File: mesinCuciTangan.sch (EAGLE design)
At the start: 9 parts, among them X1 PIR, X2 POWER, X3 IR1, X4 IR2

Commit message: Skema Beta V0.1
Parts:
- removed U$1: CP8-ADJ, userlib:CP8-ADJ
- added JP1: 12VOUTLET, pinhead:PINHD-1X5
- added JP2: GNDOUTLET, pinhead:PINHD-1X5
- added JP3: 5VOUTLET, pinhead:PINHD-1X5
- added LM2596: LM2596, userlib:CP8-ADJ
- added R1: 1K, rcl:R-US_0207/10
- added SPK_L, SPK_R: (no value), con-wago-500:W237-102
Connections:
- new net +12V: JP1.1, JP1.2, JP1.3, JP1.4, JP1.5, LM2596.IN+, X2-1.KL
- new net +5V: ARDUINO_NANO1.5V, JP3.1, JP3.2, JP3.3, JP3.4, JP3.5, LM2596.OUT+, MOD1.+5V, U$2.VCC, U$3.2, X1-1.S, X3-1.S, X4-1.S
- new net A0: ARDUINO_NANO1.ADC0/A0, U$3.4
- new net A1: ARDUINO_NANO1.ADC1/A1, U$3.5
- new net A2: ARDUINO_NANO1.ADC2/A2, U$3.6
- new net D10: ARDUINO_NANO1.D10/OC1B/!SS, U$2.TX
- new net D11: ARDUINO_NANO1.D11/MOSI, R1.1
- new net D2: ARDUINO_NANO1.D2/INT0, X1-2.S
- new net D3: ARDUINO_NANO1.D3/INT1, X3-2.S
- new net D4: ARDUINO_NANO1.D4/T0, X4-2.S
- new net GND: ARDUINO_NANO1.GND@2, JP2.1, JP2.2, JP2.3, JP2.4, JP2.5, LM2596.IN-, LM2596.OUT-, MOD1.GND@1, MOD1.GND@2, U$2.GND_1, U$3.3, X1-3.S, X2-2.KL, X3-3.S, X4-3.S
- new net N$1: MOD1.+OR, SPK_R-1.KL
- new net N$2: MOD1.IL, U$2.DAC_L
- new net N$3: MOD1.IR, U$2.DAC_R
- new net N$4: MOD1.-OR, SPK_R-2.KL
- new net N$5: MOD1.-OL, SPK_L-2.KL
- new net N$6: MOD1.+OL, SPK_L-1.KL
- new net N$7: R1.2, U$2.RX
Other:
- note added: "3 CH Relay Untuk Pompa dan Solenoid"
- note added: "Arduino NANO"
- note added: "DF Player & PAM8203"
- note added: "POWER IN & OUTLET"
- note added: "Sensor IR1"
- note added: "Sensor IR2"
- note added: "Sensor PIR"
- note added: "Sensor PIR dan IR"
- note added: "dari Power Supply"
- moved on the sheet: ARDUINO_NANO1, MOD1, U$3, X1-1, X1-2, X1-3, X2-1, X2-2, X3-1, X3-2, X3-3, X4-1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

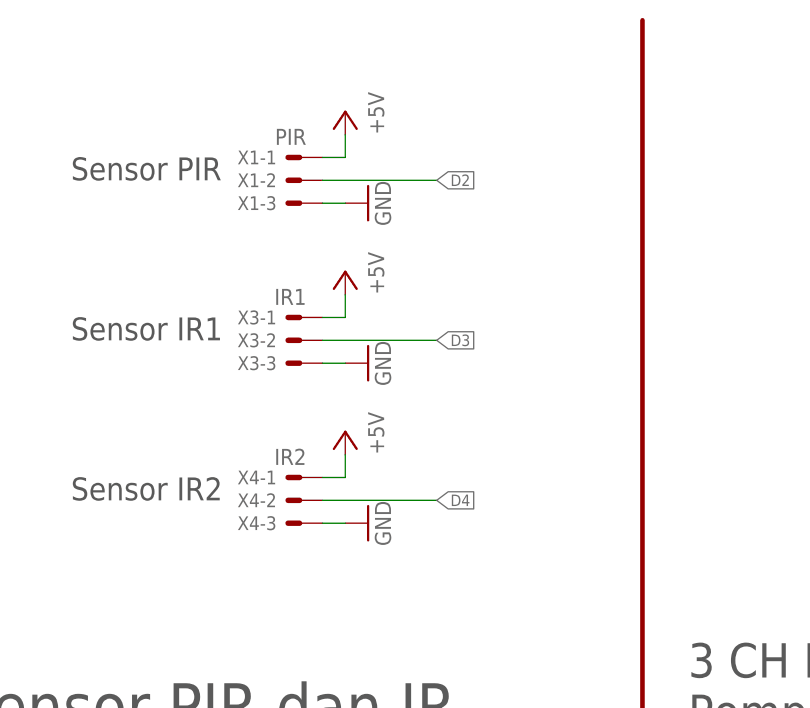
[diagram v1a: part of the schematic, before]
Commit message: simple Route Without jumper
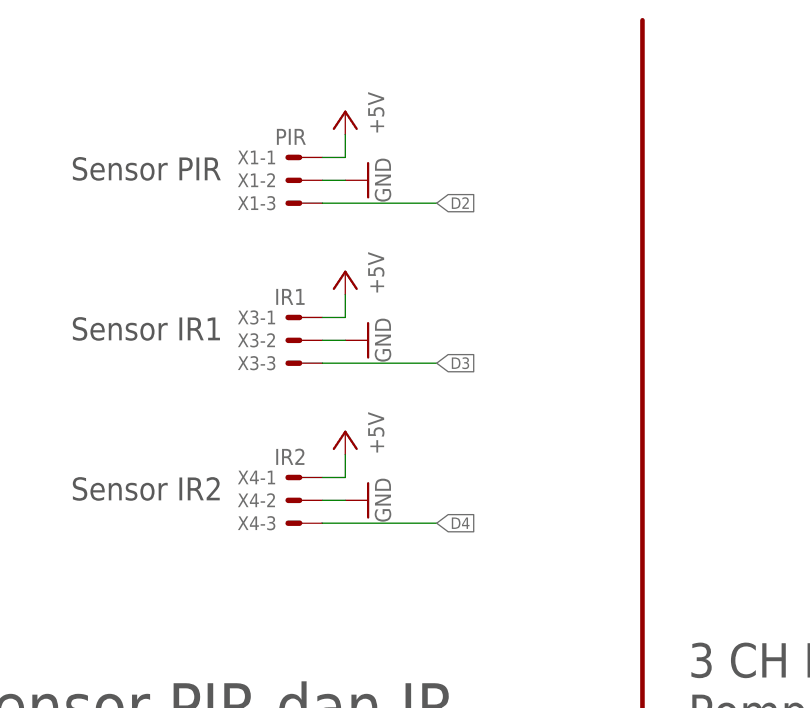
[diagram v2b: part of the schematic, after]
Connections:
- net D2: now also X1-3.S; no longer X1-2.S
- net D3: now also X3-3.S; no longer X3-2.S
- net D4: now also X4-3.S; no longer X4-2.S
- net GND: now also X1-2.S, X3-2.S, X4-2.S; no longer X1-3.S, X3-3.S, X4-3.S
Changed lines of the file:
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@@
 <setting verticaltext="up"/>
 </settings>
-<grid distance="0.1" unitdist="inch" unit="inch" style="lines" multiple="1" display="yes" altdistance="0.01" altunitdist="inch" altunit="inch"/>
+<grid distance="0.1" unitdist="inch" unit="inch" style="lines" multiple="1" display="no" altdistance="0.01" altunitdist="inch" altunit="inch"/>
 <layers>
 <layer number="1" name="Top" color="4" fill="10" visible="no" active="no"/>
@@
 <part name="LM2596" library="userlib" deviceset="CP8-ADJ" device="" value="LM2596"/>
 <part name="ARDUINO_NANO1" library="ArduinoNanoV30" deviceset="ARDUINO_NANO" device=""/>
-<part name="X2" library="con-wago-500" library_urn="urn:adsk.eagle:library:195" deviceset="W237-102" device="" package3d_urn="urn:adsk.eagle:package:10688/1" value="POWER"/>
+<part name="X2" library="con-wago-500" deviceset="W237-102" device="" package3d_urn="urn:adsk.eagle:package:10688/1" value="POWER"/>
 <part name="X3" library="con-molex" library_urn="urn:adsk.eagle:library:165" deviceset="22-23-2031" device="" package3d_urn="urn:adsk.eagle:package:8078634/1" value="IR1"/>
 <part name="X4" library="con-molex" library_urn="urn:adsk.eagle:library:165" deviceset="22-23-2031" device="" package3d_urn="urn:adsk.eagle:package:8078634/1" value="IR2"/>
@@
 <part name="GND4" library="supply1" library_urn="urn:adsk.eagle:library:371" deviceset="GND" device=""/>
 <part name="P+5" library="supply1" library_urn="urn:adsk.eagle:library:371" deviceset="+5V" device=""/>
-<part name="SPK_L" library="con-wago-500" library_urn="urn:adsk.eagle:library:195" deviceset="W237-102" device="" package3d_urn="urn:adsk.eagle:package:10688/1"/>
-<part name="SPK_R" library="con-wago-500" library_urn="urn:adsk.eagle:library:195" deviceset="W237-102" device="" package3d_urn="urn:adsk.eagle:package:10688/1"/>
+<part name="SPK_L" library="con-wago-500" deviceset="W237-102" device="" package3d_urn="urn:adsk.eagle:package:10688/1"/>
+<part name="SPK_R" library="con-wago-500" deviceset="W237-102" device="" package3d_urn="urn:adsk.eagle:package:10688/1"/>
 <part name="R1" library="rcl" deviceset="R-US_" device="0207/10" package3d_urn="urn:adsk.eagle:package:23491/2" value="1K"/>
 <part name="P+6" library="supply1" library_urn="urn:adsk.eagle:library:371" deviceset="+5V" device=""/>
@@
 <part name="P+9" library="supply1" library_urn="urn:adsk.eagle:library:371" deviceset="+5V" device=""/>
 <part name="P+10" library="supply1" library_urn="urn:adsk.eagle:library:371" deviceset="+5V" device=""/>
+<part name="P+11" library="supply1" library_urn="urn:adsk.eagle:library:371" deviceset="+5V" device=""/>
+<part name="GND10" library="supply1" library_urn="urn:adsk.eagle:library:371" deviceset="GND" device=""/>
+<part name="FRAME2" library="frames" library_urn="urn:adsk.eagle:library:229" deviceset="A4L-LOC" device=""/>
 <part name="GND7" library="supply1" library_urn="urn:adsk.eagle:library:371" deviceset="GND" device=""/>
 <part name="GND8" library="supply1" library_urn="urn:adsk.eagle:library:371" deviceset="GND" device=""/>
 <part name="GND9" library="supply1" library_urn="urn:adsk.eagle:library:371" deviceset="GND" device=""/>
-<part name="P+11" library="supply1" library_urn="urn:adsk.eagle:library:371" deviceset="+5V" device=""/>
-<part name="GND10" library="supply1" library_urn="urn:adsk.eagle:library:371" deviceset="GND" device=""/>
-<part name="FRAME2" library="frames" library_urn="urn:adsk.eagle:library:229" deviceset="A4L-LOC" device=""/>
 </parts>
 <sheets>
@@
 <attribute name="VALUE" x="152.4" y="127" size="1.778" layer="96" rot="MR90"/>
 </instance>
-<instance part="GND7" gate="1" x="152.4" y="119.38" smashed="yes" rot="R90">
-<attribute name="VALUE" x="154.94" y="116.84" size="1.778" layer="96" rot="R90"/>
-</instance>
-<instance part="GND8" gate="1" x="152.4" y="137.16" smashed="yes" rot="R90">
-<attribute name="VALUE" x="154.94" y="134.62" size="1.778" layer="96" rot="R90"/>
-</instance>
-<instance part="GND9" gate="1" x="152.4" y="154.94" smashed="yes" rot="R90">
-<attribute name="VALUE" x="154.94" y="152.4" size="1.778" layer="96" rot="R90"/>
-</instance>
 <instance part="P+11" gate="1" x="213.36" y="157.48" smashed="yes">
 <attribute name="VALUE" x="210.82" y="152.4" size="1.778" layer="96" rot="R90"/>
@@
 </instance>
 <instance part="FRAME2" gate="G$1" x="0" y="0" smashed="yes">
-<attribute name="DRAWING_NAME" x="217.17" y="15.24" size="2.54" layer="94"/>
+<attribute name="DRAWING_NAME" x="166.37" y="12.7" size="3.81" layer="94"/>
 <attribute name="LAST_DATE_TIME" x="217.17" y="10.16" size="2.286" layer="94"/>
 <attribute name="SHEET" x="230.505" y="5.08" size="2.54" layer="94"/>
+</instance>
+<instance part="GND7" gate="1" x="152.4" y="121.92" smashed="yes" rot="MR270">
+<attribute name="VALUE" x="154.94" y="124.46" size="1.778" layer="96" rot="MR270"/>
+</instance>
+<instance part="GND8" gate="1" x="152.4" y="139.7" smashed="yes" rot="MR270">
+<attribute name="VALUE" x="154.94" y="142.24" size="1.778" layer="96" rot="MR270"/>
+</instance>
+<instance part="GND9" gate="1" x="152.4" y="157.48" smashed="yes" rot="MR270">
+<attribute name="VALUE" x="154.94" y="160.02" size="1.778" layer="96" rot="MR270"/>
 </instance>
 </instances>
@@
 </segment>
 <segment>
-<pinref part="GND7" gate="1" pin="GND"/>
-<pinref part="X4" gate="-3" pin="S"/>
-<wire x1="149.86" y1="119.38" x2="147.32" y2="119.38" width="0.1524" layer="91"/>
-</segment>
-<segment>
-<pinref part="GND8" gate="1" pin="GND"/>
-<pinref part="X3" gate="-3" pin="S"/>
-<wire x1="149.86" y1="137.16" x2="147.32" y2="137.16" width="0.1524" layer="91"/>
-</segment>
-<segment>
-<pinref part="GND9" gate="1" pin="GND"/>
-<pinref part="X1" gate="-3" pin="S"/>
-<wire x1="149.86" y1="154.94" x2="147.32" y2="154.94" width="0.1524" layer="91"/>
-</segment>
-<segment>
 <pinref part="U$3" gate="G$1" pin="3"/>
 <wire x1="213.36" y1="144.78" x2="220.98" y2="144.78" width="0.1524" layer="91"/>
 <pinref part="GND10" gate="1" pin="GND"/>
+</segment>
+<segment>
+<pinref part="GND7" gate="1" pin="GND"/>
+<wire x1="149.86" y1="121.92" x2="147.32" y2="121.92" width="0.1524" layer="91"/>
+<pinref part="X4" gate="-2" pin="S"/>
+</segment>
+<segment>
+<pinref part="GND8" gate="1" pin="GND"/>
+<wire x1="149.86" y1="139.7" x2="147.32" y2="139.7" width="0.1524" layer="91"/>
+<pinref part="X3" gate="-2" pin="S"/>
+</segment>
+<segment>
+<pinref part="GND9" gate="1" pin="GND"/>
+<wire x1="149.86" y1="157.48" x2="147.32" y2="157.48" width="0.1524" layer="91"/>
+<pinref part="X1" gate="-2" pin="S"/>
 </segment>
 </net>
@@
 <net name="D2" class="0">
 <segment>
-<pinref part="X1" gate="-2" pin="S"/>
-<wire x1="147.32" y1="157.48" x2="160.02" y2="157.48" width="0.1524" layer="91"/>
-<label x="160.02" y="157.48" size="1.27" layer="95" xref="yes"/>
-</segment>
-<segment>
 <pinref part="ARDUINO_NANO1" gate="G$1" pin="D2/INT0"/>
 <wire x1="175.26" y1="68.58" x2="170.18" y2="68.58" width="0.1524" layer="91"/>
 <label x="170.18" y="68.58" size="1.27" layer="95" rot="R180" xref="yes"/>
 </segment>
+<segment>
+<wire x1="147.32" y1="154.94" x2="160.02" y2="154.94" width="0.1524" layer="91"/>
+<label x="160.02" y="154.94" size="1.27" layer="95" rot="MR180" xref="yes"/>
+<pinref part="X1" gate="-3" pin="S"/>
+</segment>
 </net>
 <net name="D3" class="0">
-<segment>
-<pinref part="X3" gate="-2" pin="S"/>
-<wire x1="147.32" y1="139.7" x2="160.02" y2="139.7" width="0.1524" layer="91"/>
-<label x="160.02" y="139.7" size="1.27" layer="95" xref="yes"/>
-</segment>
 <segment>
 <pinref part="ARDUINO_NANO1" gate="G$1" pin="D3/INT1"/>
@@
 <label x="170.18" y="66.04" size="1.27" layer="95" rot="R180" xref="yes"/>
 </segment>
+<segment>
+<wire x1="147.32" y1="137.16" x2="160.02" y2="137.16" width="0.1524" layer="91"/>
+<label x="160.02" y="137.16" size="1.27" layer="95" rot="MR180" xref="yes"/>
+<pinref part="X3" gate="-3" pin="S"/>
+</segment>
 </net>
 <net name="D4" class="0">
-<segment>
-<pinref part="X4" gate="-2" pin="S"/>
-<wire x1="147.32" y1="121.92" x2="160.02" y2="121.92" width="0.1524" layer="91"/>
-<label x="160.02" y="121.92" size="1.27" layer="95" xref="yes"/>
-</segment>
 <segment>
 <pinref part="ARDUINO_NANO1" gate="G$1" pin="D4/T0"/>
@@
 <label x="170.18" y="63.5" size="1.27" layer="95" rot="R180" xref="yes"/>
 </segment>
-</net>
+<segment>
+<wire x1="147.32" y1="119.38" x2="160.02" y2="119.38" width="0.1524" layer="91"/>
+<label x="160.02" y="119.38" size="1.27" layer="95" rot="MR180" xref="yes"/>
+<pinref part="X4" gate="-3" pin="S"/>
+</segment>
+</net>

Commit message: pcb coba ceta #1
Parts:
- renumbered MOD1 to PAM8403
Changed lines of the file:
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@@
 <part name="X4" library="con-molex" library_urn="urn:adsk.eagle:library:165" deviceset="22-23-2031" device="" package3d_urn="urn:adsk.eagle:package:8078634/1" value="IR2"/>
 <part name="U$2" library="DFPlayer_v1" deviceset="DFPLAYER" device=""/>
-<part name="MOD1" library="dl9sec_public" deviceset="PAM8403MOD" device="-F2"/>
+<part name="PAM8403" library="dl9sec_public" deviceset="PAM8403MOD" device="-F2"/>
 <part name="U$3" library="mesinCuciCustomLib" deviceset="3CHANNELRELAY5V" device=""/>
 <part name="P+1" library="supply1" library_urn="urn:adsk.eagle:library:371" deviceset="+12V" device=""/>
@@
 </instance>
 <instance part="U$2" gate="G$1" x="66.04" y="71.12" smashed="yes"/>
-<instance part="MOD1" gate="G$1" x="55.88" y="25.4" smashed="yes">
+<instance part="PAM8403" gate="G$1" x="55.88" y="25.4" smashed="yes">
 <attribute name="NAME" x="55.88" y="44.45" size="1.27" layer="95"/>
 <attribute name="VALUE" x="69.85" y="44.45" size="1.27" layer="96"/>
@@
 </segment>
 <segment>
-<pinref part="MOD1" gate="G$1" pin="GND@2"/>
+<pinref part="PAM8403" gate="G$1" pin="GND@2"/>
 <wire x1="68.58" y1="22.86" x2="68.58" y2="17.78" width="0.1524" layer="91"/>
 <wire x1="68.58" y1="17.78" x2="66.04" y2="17.78" width="0.1524" layer="91"/>
-<pinref part="MOD1" gate="G$1" pin="GND@1"/>
+<pinref part="PAM8403" gate="G$1" pin="GND@1"/>
 <wire x1="66.04" y1="17.78" x2="66.04" y2="22.86" width="0.1524" layer="91"/>
 <pinref part="GND4" gate="1" pin="GND"/>
@@
 </segment>
 <segment>
-<pinref part="MOD1" gate="G$1" pin="+5V"/>
+<pinref part="PAM8403" gate="G$1" pin="+5V"/>
 <pinref part="P+4" gate="1" pin="+5V"/>
 <wire x1="67.31" y1="45.72" x2="67.31" y2="50.546" width="0.1524" layer="91"/>
@@
 <segment>
 <pinref part="SPK_R" gate="-1" pin="KL"/>
-<pinref part="MOD1" gate="G$1" pin="+OR"/>
+<pinref part="PAM8403" gate="G$1" pin="+OR"/>
 <wire x1="96.52" y1="30.48" x2="81.28" y2="30.48" width="0.1524" layer="91"/>
 </segment>
@@
 <segment>
 <pinref part="SPK_R" gate="-2" pin="KL"/>
-<pinref part="MOD1" gate="G$1" pin="-OR"/>
+<pinref part="PAM8403" gate="G$1" pin="-OR"/>
 <wire x1="96.52" y1="25.4" x2="96.52" y2="27.94" width="0.1524" layer="91"/>
 <wire x1="96.52" y1="27.94" x2="81.28" y2="27.94" width="0.1524" layer="91"/>
@@
 <net name="N$5" class="0">
 <segment>
-<pinref part="MOD1" gate="G$1" pin="-OL"/>
+<pinref part="PAM8403" gate="G$1" pin="-OL"/>
 <pinref part="SPK_L" gate="-2" pin="KL"/>
 <wire x1="81.28" y1="38.1" x2="96.52" y2="38.1" width="0.1524" layer="91"/>
@@
 <segment>
 <pinref part="SPK_L" gate="-1" pin="KL"/>
-<pinref part="MOD1" gate="G$1" pin="+OL"/>
+<pinref part="PAM8403" gate="G$1" pin="+OL"/>
 <wire x1="96.52" y1="43.18" x2="96.52" y2="40.64" width="0.1524" layer="91"/>
 <wire x1="96.52" y1="40.64" x2="81.28" y2="40.64" width="0.1524" layer="91"/>
@@
 <net name="N$2" class="0">
 <segment>
-<pinref part="MOD1" gate="G$1" pin="IL"/>
+<pinref part="PAM8403" gate="G$1" pin="IL"/>
 <wire x1="53.34" y1="35.56" x2="35.56" y2="35.56" width="0.1524" layer="91"/>
 <wire x1="35.56" y1="35.56" x2="35.56" y2="71.12" width="0.1524" layer="91"/>
@@
 <wire x1="48.26" y1="73.66" x2="33.02" y2="73.66" width="0.1524" layer="91"/>
 <wire x1="33.02" y1="73.66" x2="33.02" y2="33.02" width="0.1524" layer="91"/>
-<pinref part="MOD1" gate="G$1" pin="IR"/>
+<pinref part="PAM8403" gate="G$1" pin="IR"/>
 <wire x1="33.02" y1="33.02" x2="53.34" y2="33.02" width="0.1524" layer="91"/>
 </segment>

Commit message: commit with code
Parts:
- removed SPK_L: (no value), con-wago-500:W237-102
- X3, X4: device con-molex:22-23-2031 -> con-molex:22-23-2041
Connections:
- removed net N$5: PAM8403.-OL, SPK_L-2.KL
- removed net N$6: PAM8403.+OL, SPK_L-1.KL
- new net D5: ARDUINO_NANO1.D5/T1, X4-3.S
- new net D6: ARDUINO_NANO1.D6/AIN0, X4-4.S
- net D4: now also X3-4.S; no longer X4-3.S
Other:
- note added: "Ping1"
- note added: "Ping2"
- note removed: "Sensor IR1"
- note removed: "Sensor IR2"
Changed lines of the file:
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@@
 <part name="ARDUINO_NANO1" library="ArduinoNanoV30" deviceset="ARDUINO_NANO" device=""/>
 <part name="X2" library="con-wago-500" deviceset="W237-102" device="" package3d_urn="urn:adsk.eagle:package:10688/1" value="POWER"/>
-<part name="X3" library="con-molex" library_urn="urn:adsk.eagle:library:165" deviceset="22-23-2031" device="" package3d_urn="urn:adsk.eagle:package:8078634/1" value="IR1"/>
-<part name="X4" library="con-molex" library_urn="urn:adsk.eagle:library:165" deviceset="22-23-2031" device="" package3d_urn="urn:adsk.eagle:package:8078634/1" value="IR2"/>
+<part name="X3" library="con-molex" library_urn="urn:adsk.eagle:library:165" deviceset="22-23-2041" device="" package3d_urn="urn:adsk.eagle:package:8078635/1" value="IR1"/>
+<part name="X4" library="con-molex" library_urn="urn:adsk.eagle:library:165" deviceset="22-23-2041" device="" package3d_urn="urn:adsk.eagle:package:8078635/1" value="IR2"/>
 <part name="U$2" library="DFPlayer_v1" deviceset="DFPLAYER" device=""/>
 <part name="PAM8403" library="dl9sec_public" deviceset="PAM8403MOD" device="-F2"/>
@@
 <part name="GND4" library="supply1" library_urn="urn:adsk.eagle:library:371" deviceset="GND" device=""/>
 <part name="P+5" library="supply1" library_urn="urn:adsk.eagle:library:371" deviceset="+5V" device=""/>
-<part name="SPK_L" library="con-wago-500" deviceset="W237-102" device="" package3d_urn="urn:adsk.eagle:package:10688/1"/>
 <part name="SPK_R" library="con-wago-500" deviceset="W237-102" device="" package3d_urn="urn:adsk.eagle:package:10688/1"/>
 <part name="R1" library="rcl" deviceset="R-US_" device="0207/10" package3d_urn="urn:adsk.eagle:package:23491/2" value="1K"/>
@@
 Supply</text>
 <text x="119.38" y="157.48" size="2.54" layer="97">Sensor PIR</text>
-<text x="119.38" y="139.7" size="2.54" layer="97">Sensor IR1</text>
-<text x="119.38" y="121.92" size="2.54" layer="97">Sensor IR2</text>
+<text x="127" y="139.7" size="2.54" layer="97">Ping1</text>
+<text x="127" y="121.92" size="2.54" layer="97">Ping2</text>
 <wire x1="5.08" y1="93.98" x2="104.14" y2="93.98" width="0.508" layer="94"/>
 <wire x1="104.14" y1="93.98" x2="129.54" y2="93.98" width="0.508" layer="94"/>
@@
 <attribute name="VALUE" x="44.45" y="83.566" size="1.778" layer="96" rot="R90"/>
 </instance>
-<instance part="SPK_L" gate="-1" x="101.6" y="43.18" smashed="yes" rot="MR0">
-<attribute name="NAME" x="101.6" y="44.069" size="1.778" layer="95" rot="MR180"/>
-</instance>
-<instance part="SPK_L" gate="-2" x="101.6" y="38.1" smashed="yes" rot="MR0">
-<attribute name="VALUE" x="104.14" y="34.417" size="1.778" layer="96" rot="MR0"/>
-<attribute name="NAME" x="101.6" y="38.989" size="1.778" layer="95" rot="MR180"/>
-</instance>
 <instance part="SPK_R" gate="-1" x="101.6" y="30.48" smashed="yes" rot="MR0">
 <attribute name="NAME" x="101.6" y="31.369" size="1.778" layer="95" rot="MR180"/>
@@
 <instance part="GND9" gate="1" x="152.4" y="157.48" smashed="yes" rot="MR270">
 <attribute name="VALUE" x="154.94" y="160.02" size="1.778" layer="96" rot="MR270"/>
+</instance>
+<instance part="X3" gate="-4" x="144.78" y="134.62" smashed="yes" rot="R180">
+<attribute name="NAME" x="142.24" y="135.382" size="1.524" layer="95" rot="R180"/>
+</instance>
+<instance part="X4" gate="-4" x="144.78" y="116.84" smashed="yes" rot="R180">
+<attribute name="NAME" x="142.24" y="117.602" size="1.524" layer="95" rot="R180"/>
 </instance>
 </instances>
@@
 </segment>
 </net>
-<net name="N$5" class="0">
-<segment>
-<pinref part="PAM8403" gate="G$1" pin="-OL"/>
-<pinref part="SPK_L" gate="-2" pin="KL"/>
-<wire x1="81.28" y1="38.1" x2="96.52" y2="38.1" width="0.1524" layer="91"/>
-</segment>
-</net>
-<net name="N$6" class="0">
-<segment>
-<pinref part="SPK_L" gate="-1" pin="KL"/>
-<pinref part="PAM8403" gate="G$1" pin="+OL"/>
-<wire x1="96.52" y1="43.18" x2="96.52" y2="40.64" width="0.1524" layer="91"/>
-<wire x1="96.52" y1="40.64" x2="81.28" y2="40.64" width="0.1524" layer="91"/>
-</segment>
-</net>
 <net name="D10" class="0">
 <segment>
@@
 </segment>
 <segment>
-<wire x1="147.32" y1="119.38" x2="160.02" y2="119.38" width="0.1524" layer="91"/>
-<label x="160.02" y="119.38" size="1.27" layer="95" rot="MR180" xref="yes"/>
-<pinref part="X4" gate="-3" pin="S"/>
+<wire x1="147.32" y1="134.62" x2="160.02" y2="134.62" width="0.1524" layer="91"/>
+<label x="160.02" y="134.62" size="1.27" layer="95" rot="MR180" xref="yes"/>
+<pinref part="X3" gate="-4" pin="S"/>
 </segment>
 </net>
@@
 </segment>
 </net>
+<net name="D5" class="0">
+<segment>
+<wire x1="170.18" y1="60.96" x2="175.26" y2="60.96" width="0.1524" layer="91"/>
+<label x="170.18" y="60.96" size="1.27" layer="95" rot="R180" xref="yes"/>
+<pinref part="ARDUINO_NANO1" gate="G$1" pin="D5/T1"/>
+</segment>
+<segment>
+<wire x1="160.02" y1="119.38" x2="147.32" y2="119.38" width="0.1524" layer="91"/>
+<label x="160.02" y="119.38" size="1.27" layer="95" rot="MR180" xref="yes"/>
+<pinref part="X4" gate="-3" pin="S"/>
+</segment>
+</net>
+<net name="D6" class="0">
+<segment>
+<wire x1="175.26" y1="58.42" x2="170.18" y2="58.42" width="0.1524" layer="91"/>
+<label x="170.18" y="58.42" size="1.27" layer="95" rot="R180" xref="yes"/>
+<pinref part="ARDUINO_NANO1" gate="G$1" pin="D6/AIN0"/>
+</segment>
+<segment>
+<wire x1="147.32" y1="116.84" x2="160.02" y2="116.84" width="0.1524" layer="91"/>
+<label x="160.02" y="116.84" size="1.27" layer="95" rot="MR180" xref="yes"/>
+<pinref part="X4" gate="-4" pin="S"/>
+</segment>
+</net>
